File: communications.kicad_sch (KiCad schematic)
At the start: 12 parts, among them U41 DS90LV048ATMTCX_NOPB, U42 DS90LV047ATMTCX_NOPB

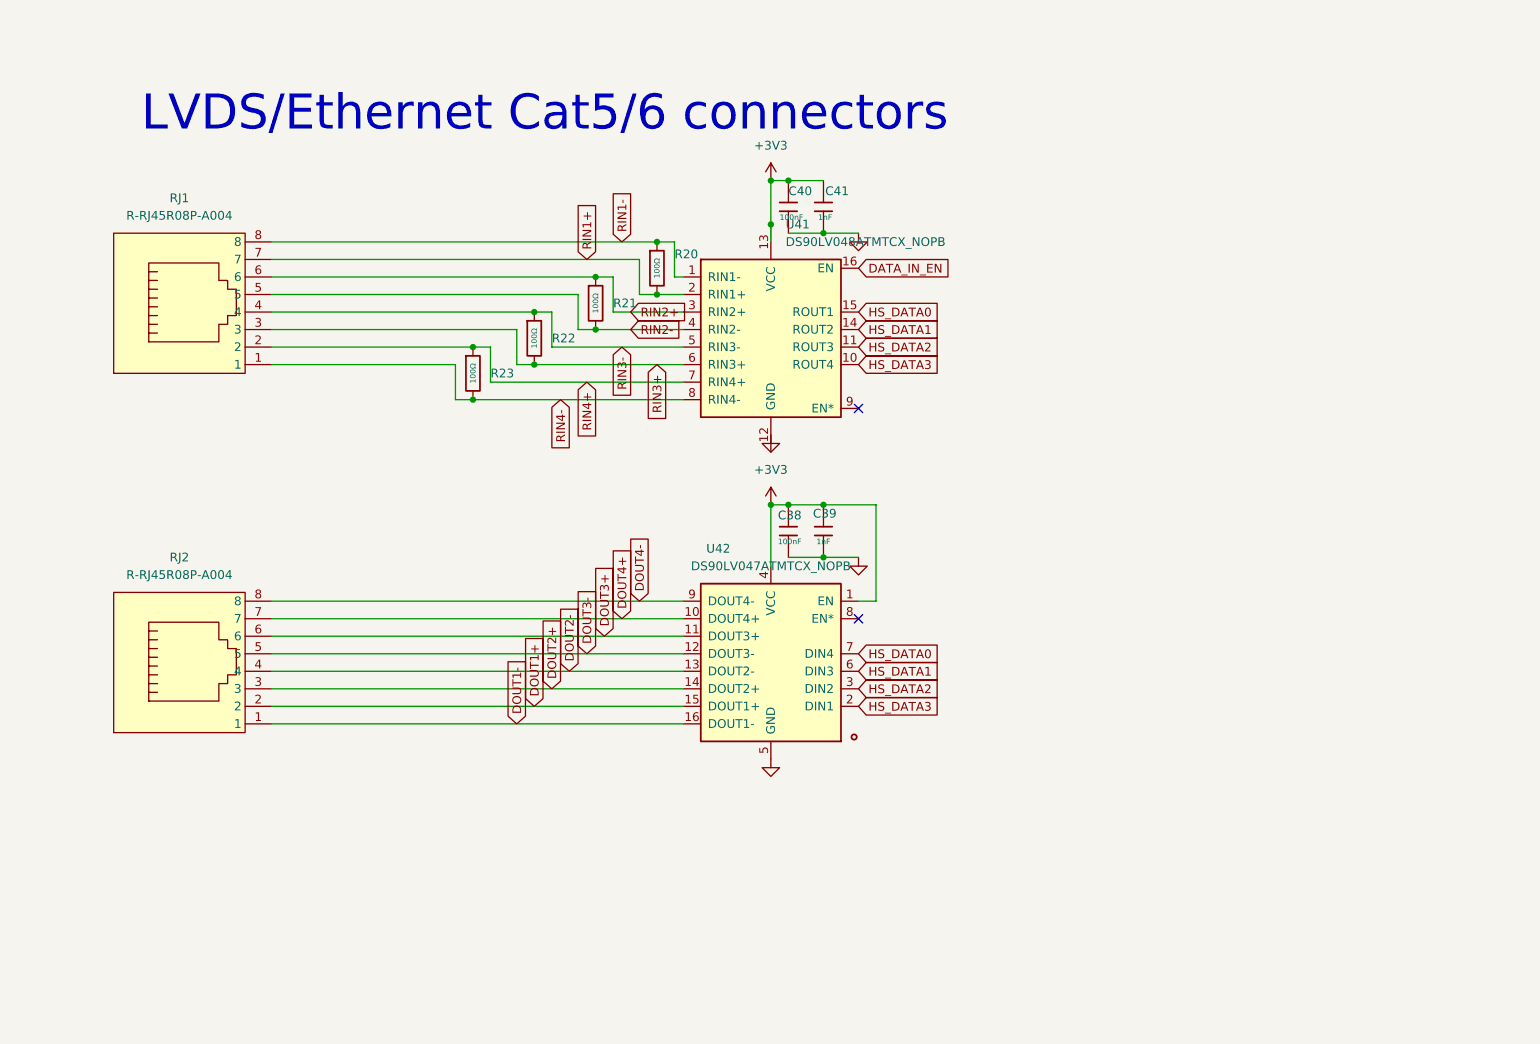
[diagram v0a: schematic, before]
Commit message: Bundle 3D models in the project, add board renders to the README
The board's models were referenced through KICAD_3RD_PARTY,
KICAD8_3RD_PARTY and KICAD9_3DMODEL_DIR, which KiCad 10 doesn't define, so
most parts showed no 3D model. Copy all 38 into 3dmodels/ and point the
board and the project footprint libraries at ${KIPRJMOD}/3dmodels.

Also includes pending library and schematic edits, and ignores KiCad's
.history/ folder.

Co-Authored-By: Claude Opus 5.5 <noreply@anthropic.com>
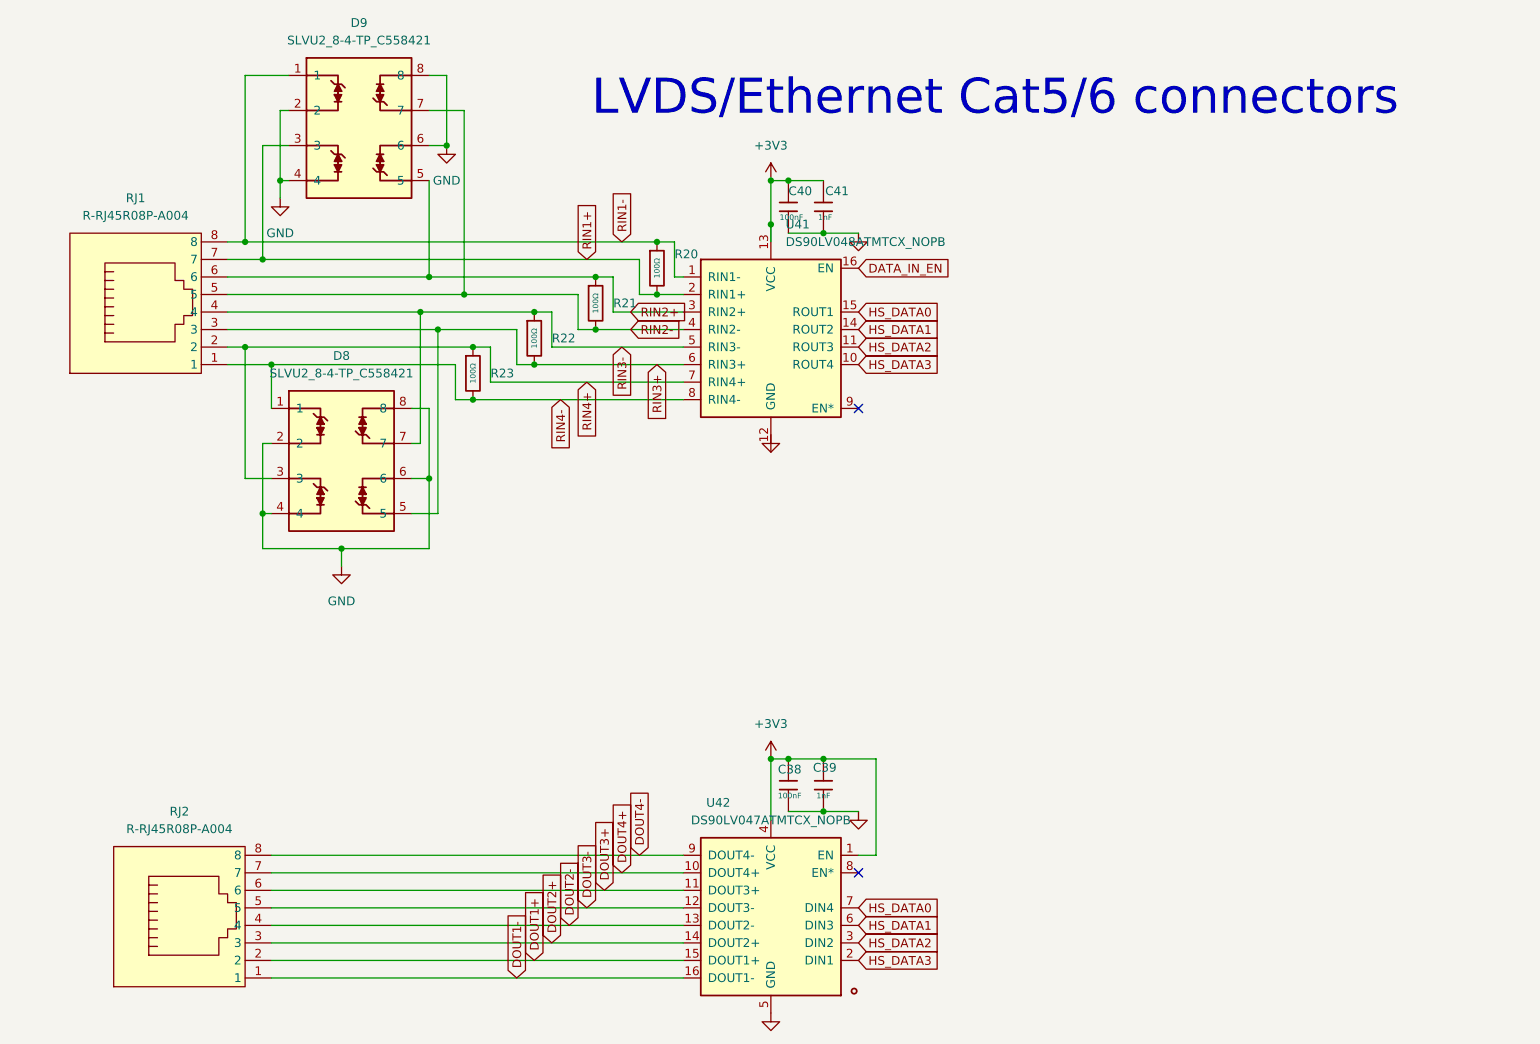
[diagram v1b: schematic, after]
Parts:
- added D8, D9: SLVU2_8-4-TP_C558421, JLCImport:SLVU2_8-4-TP_C558421, symbol JLCImport:SLVU2_8-4-TP_C558421
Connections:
- net GND: now also D8.2, D8.4, D8.6, D8.8, D9.2, D9.4, D9.6, D9.8
- net RIN1+: now also D9.3
- net RIN1-: now also D9.1
- net RIN2+: now also D9.5
- net RIN2-: now also D9.7
- net RIN3+: now also D8.5
- net RIN3-: now also D8.7
- net RIN4+: now also D8.3
- net RIN4-: now also D8.1
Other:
- moved on the sheet: C38, C39, RJ1, RJ2, U42
